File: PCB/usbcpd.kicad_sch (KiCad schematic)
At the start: 24 parts, among them J4 USB_C_Receptacle_USB2.0, Q2 SSM6J507NU, U1 STUSB4500QTR

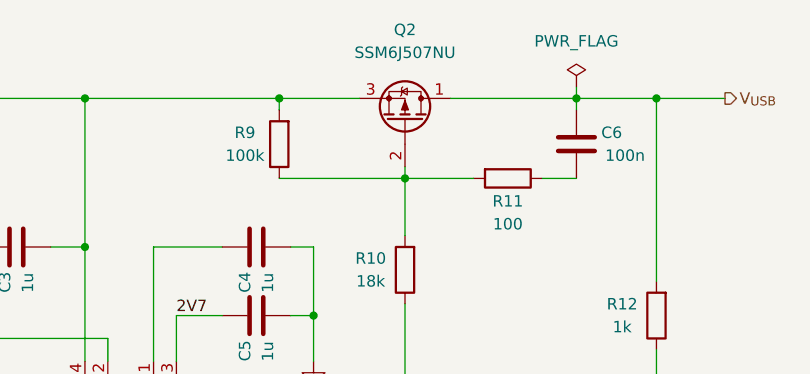
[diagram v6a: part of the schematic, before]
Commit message: Resistors ok in BOM
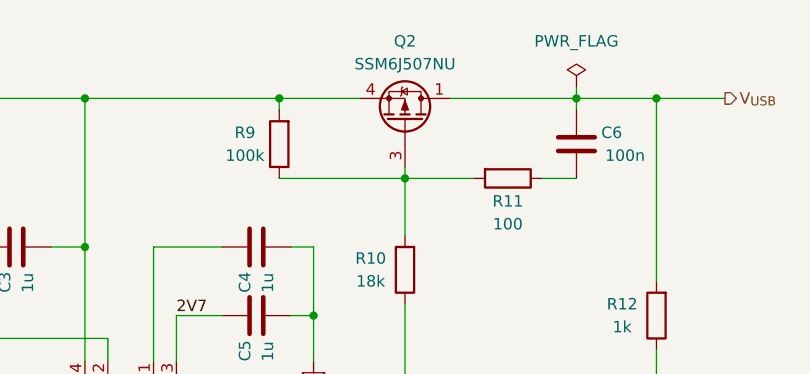
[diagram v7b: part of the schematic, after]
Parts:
- removed Q2: SSM6J507NU, symbol Device:Q_PMOS_DGS
- added Q2: SSM6J507NU, TattooSupplyFootprints:TRANS_SSM6J507NU,LF, symbol TattooSupplyLib:PMOS_Toshiba_UDFN8
- R10: footprint (none) -> Resistor_SMD:R_0603_1608Metric; MPN (none) -> ERJ-3EKF1802V; Manufacturer (none) -> Panasonic
- R11: footprint (none) -> Resistor_SMD:R_0603_1608Metric; MPN (none) -> ERJ-3EKF1000V; Manufacturer (none) -> Panasonic
- R12, R7: footprint (none) -> Resistor_SMD:R_0603_1608Metric; MPN (none) -> ERJ-3EKF1001V; Manufacturer (none) -> Panasonic
- R4: footprint (none) -> Resistor_SMD:R_0603_1608Metric; MPN (none) -> ERJ-3EKF4700V; Manufacturer (none) -> Panasonic
- R5, R6, R8, R9: footprint (none) -> Resistor_SMD:R_0603_1608Metric; MPN (none) -> ERJ-3EKF1003V; Manufacturer (none) -> Panasonic
- U1: MPN (none) -> STUSB4500QTR; Manufacturer (none) -> STMicroelectronics
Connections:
- net V_{USB}: now also Q2.1 (D), Q2.2 (D), Q2.5 (D), Q2.6 (D), Q2.7 (D)
- net v_{USB}: now also Q2.4 (S), Q2.8 (S)
- net at R10.2, R11.2, R9.1: now also Q2.3 (G)
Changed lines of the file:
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@@
       (effects (font (size 1.27 1.27)))
     )
-    (property "Footprint" "" (at 212.598 66.04 90)
+    (property "Footprint" "Resistor_SMD:R_0603_1608Metric" (at 212.598 66.04 90)
       (effects (font (size 1.27 1.27)) hide)
     )
@@
       (effects (font (size 1.27 1.27)) hide)
     )
-    (property "MPN" "" (at 210.82 66.04 0)
-      (effects (font (size 1.27 1.27)) hide)
-    )
-    (property "Manufacturer" "" (at 210.82 66.04 0)
+    (property "MPN" "ERJ-3EKF1003V" (at 210.82 66.04 0)
+      (effects (font (size 1.27 1.27)) hide)
+    )
+    (property "Manufacturer" "Panasonic" (at 210.82 66.04 0)
       (effects (font (size 1.27 1.27)) hide)
     )
@@
       (effects (font (size 1.27 1.27)))
     )
-    (property "Footprint" "" (at 166.878 137.16 90)
+    (property "Footprint" "Resistor_SMD:R_0603_1608Metric" (at 166.878 137.16 90)
       (effects (font (size 1.27 1.27)) hide)
     )
@@
       (effects (font (size 1.27 1.27)) hide)
     )
-    (property "MPN" "" (at 165.1 137.16 0)
-      (effects (font (size 1.27 1.27)) hide)
-    )
-    (property "Manufacturer" "" (at 165.1 137.16 0)
+    (property "MPN" "ERJ-3EKF1003V" (at 165.1 137.16 0)
+      (effects (font (size 1.27 1.27)) hide)
+    )
+    (property "Manufacturer" "Panasonic" (at 165.1 137.16 0)
       (effects (font (size 1.27 1.27)) hide)
     )
@@
       (effects (font (size 1.27 1.27)))
     )
-    (property "Footprint" "" (at 175.768 137.16 90)
+    (property "Footprint" "Resistor_SMD:R_0603_1608Metric" (at 175.768 137.16 90)
       (effects (font (size 1.27 1.27)) hide)
     )
@@
       (effects (font (size 1.27 1.27)) hide)
     )
-    (property "MPN" "" (at 173.99 137.16 0)
-      (effects (font (size 1.27 1.27)) hide)
-    )
-    (property "Manufacturer" "" (at 173.99 137.16 0)
+    (property "MPN" "ERJ-3EKF1003V" (at 173.99 137.16 0)
+      (effects (font (size 1.27 1.27)) hide)
+    )
+    (property "Manufacturer" "Panasonic" (at 173.99 137.16 0)
       (effects (font (size 1.27 1.27)) hide)
     )
@@
       (effects (font (size 1.27 1.27)) hide)
     )
-    (property "MPN" "" (at 191.77 113.03 0)
-      (effects (font (size 1.27 1.27)) hide)
-    )
-    (property "Manufacturer" "" (at 191.77 113.03 0)
+    (property "MPN" "STUSB4500QTR" (at 191.77 113.03 0)
+      (effects (font (size 1.27 1.27)) hide)
+    )
+    (property "Manufacturer" "STMicroelectronics " (at 191.77 113.03 0)
       (effects (font (size 1.27 1.27)) hide)
     )
@@
     )
   )
+  (symbol (lib_id "TattooSupplyLib:PMOS_Toshiba_UDFN8") (at 224.79 63.5 270) (mirror x) (unit 1)
+    (in_bom yes) (on_board yes) (dnp no) (fields_autoplaced)
+    (property "Reference" "Q2" (at 224.79 54.61 90)
+      (effects (font (size 1.27 1.27)))
+    )
+    (property "Value" "SSM6J507NU" (at 224.79 57.15 90)
+      (effects (font (size 1.27 1.27)))
+    )
+    (property "Footprint" "TattooSupplyFootprints:TRANS_SSM6J507NU,LF" (at 227.33 58.42 0)
+      (effects (font (size 1.27 1.27)) hide)
+    )
+    (property "Datasheet" "~" (at 224.79 63.5 0)
+      (effects (font (size 1.27 1.27)) hide)
+    )
+    (property "MPN" "SSM6J507NU" (at 224.79 63.5 0)
+      (effects (font (size 1.27 1.27)) hide)
+    )
+    (property "Manufacturer" "Toshiba" (at 224.79 63.5 0)
+      (effects (font (size 1.27 1.27)) hide)
+    )
+    (pin "1")
+    (pin "2")
+    (pin "3")
+    (pin "4")
+    (pin "5")
+    (pin "6")
+    (pin "7")
+    (pin "8")
+    (instances
+      (project "Tattoo_Supply"
+        (path "/036b57f3-323c-4da7-bad2-1c27fa1415e1/53d1b181-b4e9-4f58-bcbd-a7e6cd4ea6ab"
+          (reference "Q2") (unit 1)
+        )
+      )
+    )
+  )
   (symbol (lib_id "Power_Protection:RCLAMP0502B") (at 57.15 167.64 90) (unit 1)
     (in_bom yes) (on_board yes) (dnp no) (fields_autoplaced)
@@
       (effects (font (size 1.27 1.27)))
     )
-    (property "Footprint" "" (at 170.18 117.348 90)
+    (property "Footprint" "Resistor_SMD:R_0603_1608Metric" (at 170.18 117.348 90)
       (effects (font (size 1.27 1.27)) hide)
     )
@@
       (effects (font (size 1.27 1.27)) hide)
     )
-    (property "MPN" "" (at 170.18 115.57 0)
-      (effects (font (size 1.27 1.27)) hide)
-    )
-    (property "Manufacturer" "" (at 170.18 115.57 0)
+    (property "MPN" "ERJ-3EKF1001V" (at 170.18 115.57 0)
+      (effects (font (size 1.27 1.27)) hide)
+    )
+    (property "Manufacturer" "Panasonic" (at 170.18 115.57 0)
       (effects (font (size 1.27 1.27)) hide)
     )
@@
     )
   )
-  (symbol (lib_id "Device:Q_PMOS_DGS") (at 224.79 63.5 270) (mirror x) (unit 1)
-    (in_bom yes) (on_board yes) (dnp no) (fields_autoplaced)
-    (property "Reference" "Q2" (at 224.79 53.34 90)
-      (effects (font (size 1.27 1.27)))
-    )
-    (property "Value" "SSM6J507NU" (at 224.79 55.88 90)
-      (effects (font (size 1.27 1.27)))
-    )
-    (property "Footprint" "" (at 227.33 58.42 0)
-      (effects (font (size 1.27 1.27)) hide)
-    )
-    (property "Datasheet" "~" (at 224.79 63.5 0)
-      (effects (font (size 1.27 1.27)) hide)
-    )
-    (property "MPN" "" (at 224.79 63.5 0)
-      (effects (font (size 1.27 1.27)) hide)
-    )
-    (property "Manufacturer" "" (at 224.79 63.5 0)
-      (effects (font (size 1.27 1.27)) hide)
-    )
-    (pin "1")
-    (pin "2")
-    (pin "3")
-    (instances
-      (project "Tattoo_Supply"
-        (path "/036b57f3-323c-4da7-bad2-1c27fa1415e1/53d1b181-b4e9-4f58-bcbd-a7e6cd4ea6ab"
-          (reference "Q2") (unit 1)
-        )
-      )
-    )
-  )
   (symbol (lib_id "power:GND") (at 143.51 124.46 0) (unit 1)
     (in_bom yes) (on_board yes) (dnp no)
@@
       (effects (font (size 1.27 1.27)))
     )
-    (property "Footprint" "" (at 226.568 80.01 90)
+    (property "Footprint" "Resistor_SMD:R_0603_1608Metric" (at 226.568 80.01 90)
       (effects (font (size 1.27 1.27)) hide)
     )
@@
       (effects (font (size 1.27 1.27)) hide)
     )
-    (property "MPN" "" (at 224.79 80.01 0)
-      (effects (font (size 1.27 1.27)) hide)
-    )
-    (property "Manufacturer" "" (at 224.79 80.01 0)
+    (property "MPN" "ERJ-3EKF1802V" (at 224.79 80.01 0)
+      (effects (font (size 1.27 1.27)) hide)
+    )
+    (property "Manufacturer" "Panasonic" (at 224.79 80.01 0)
       (effects (font (size 1.27 1.27)) hide)
     )
@@
       (effects (font (size 1.27 1.27)))
     )
-    (property "Footprint" "" (at 236.22 68.072 90)
+    (property "Footprint" "Resistor_SMD:R_0603_1608Metric" (at 236.22 68.072 90)
       (effects (font (size 1.27 1.27)) hide)
     )
@@
       (effects (font (size 1.27 1.27)) hide)
     )
-    (property "MPN" "" (at 236.22 69.85 0)
-      (effects (font (size 1.27 1.27)) hide)
-    )
-    (property "Manufacturer" "" (at 236.22 69.85 0)
+    (property "MPN" "ERJ-3EKF1000V" (at 236.22 69.85 0)
+      (effects (font (size 1.27 1.27)) hide)
+    )
+    (property "Manufacturer" "Panasonic" (at 236.22 69.85 0)
       (effects (font (size 1.27 1.27)) hide)
     )
@@
       (effects (font (size 1.27 1.27)))
     )
-    (property "Footprint" "" (at 151.892 109.22 90)
+    (property "Footprint" "Resistor_SMD:R_0603_1608Metric" (at 151.892 109.22 90)
       (effects (font (size 1.27 1.27)) hide)
     )
@@
       (effects (font (size 1.27 1.27)) hide)
     )
-    (property "MPN" "" (at 153.67 109.22 0)
-      (effects (font (size 1.27 1.27)) hide)
-    )
-    (property "Manufacturer" "" (at 153.67 109.22 0)
+    (property "MPN" "ERJ-3EKF4700V" (at 153.67 109.22 0)
+      (effects (font (size 1.27 1.27)) hide)
+    )
+    (property "Manufacturer" "Panasonic" (at 153.67 109.22 0)
       (effects (font (size 1.27 1.27)) hide)
     )
@@
       (effects (font (size 1.27 1.27)))
     )
-    (property "Footprint" "" (at 164.338 100.33 90)
+    (property "Footprint" "Resistor_SMD:R_0603_1608Metric" (at 164.338 100.33 90)
       (effects (font (size 1.27 1.27)) hide)
     )
@@
       (effects (font (size 1.27 1.27)) hide)
     )
-    (property "MPN" "" (at 162.56 100.33 0)
-      (effects (font (size 1.27 1.27)) hide)
-    )
-    (property "Manufacturer" "" (at 162.56 100.33 0)
+    (property "MPN" "ERJ-3EKF1003V" (at 162.56 100.33 0)
+      (effects (font (size 1.27 1.27)) hide)
+    )
+    (property "Manufacturer" "Panasonic" (at 162.56 100.33 0)
       (effects (font (size 1.27 1.27)) hide)
     )
@@
       (effects (font (size 1.27 1.27)))
     )
-    (property "Footprint" "" (at 254.508 85.09 90)
+    (property "Footprint" "Resistor_SMD:R_0603_1608Metric" (at 254.508 85.09 90)
       (effects (font (size 1.27 1.27)) hide)
     )
@@
       (effects (font (size 1.27 1.27)) hide)
     )
-    (property "MPN" "" (at 252.73 85.09 0)
-      (effects (font (size 1.27 1.27)) hide)
-    )
-    (property "Manufacturer" "" (at 252.73 85.09 0)
-      (effects (font (size 1.27 1.27)) hide)
-    )
+    (property "MPN" "ERJ-3EKF1001V" (at 252.73 85.09 0)
+      (effects (font (size 1.27 1.27)) hide)
+    )
+    (property "Manufacturer" "Panasonic" (at 252.73 85.09 0)
+      (effects (font (size 1.27 1.27)) hide)
+    )

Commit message: continue bom
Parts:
- J4: footprint (none) -> Connector_USB:USB_C_Receptacle_GCT_USB4105-xx-A_16P_TopMnt_Horizontal; MPN (none) -> GCT; Manufacturer (none) -> USB4105-GF-A
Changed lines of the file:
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@@
       (effects (font (size 1.27 1.27)))
     )
-    (property "Footprint" "" (at 53.34 114.3 0)
+    (property "Footprint" "Connector_USB:USB_C_Receptacle_GCT_USB4105-xx-A_16P_TopMnt_Horizontal" (at 53.34 114.3 0)
       (effects (font (size 1.27 1.27)) hide)
     )
-    (property "Datasheet" "https://www.usb.org/sites/default/files/documents/usb_type-c.zip" (at 53.34 114.3 0)
+    (property "Datasheet" "" (at 53.34 114.3 0)
       (effects (font (size 1.27 1.27)) hide)
     )
-    (property "MPN" "" (at 49.53 114.3 0)
+    (property "MPN" "GCT" (at 49.53 114.3 0)
       (effects (font (size 1.27 1.27)) hide)
     )
-    (property "Manufacturer" "" (at 49.53 114.3 0)
+    (property "Manufacturer" "USB4105-GF-A" (at 49.53 114.3 0)
       (effects (font (size 1.27 1.27)) hide)
     )
